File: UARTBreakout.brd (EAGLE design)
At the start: 21.6 x 16.5 mm, 0 parts

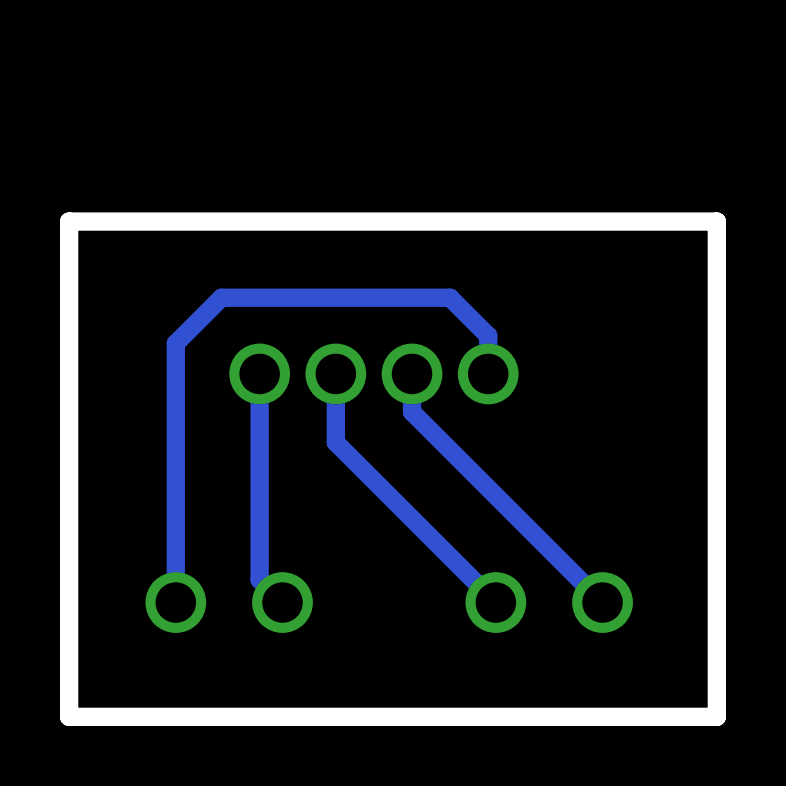
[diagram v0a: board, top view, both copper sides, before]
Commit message: Made both breakout boards REALLY aesthetic, also they self document now
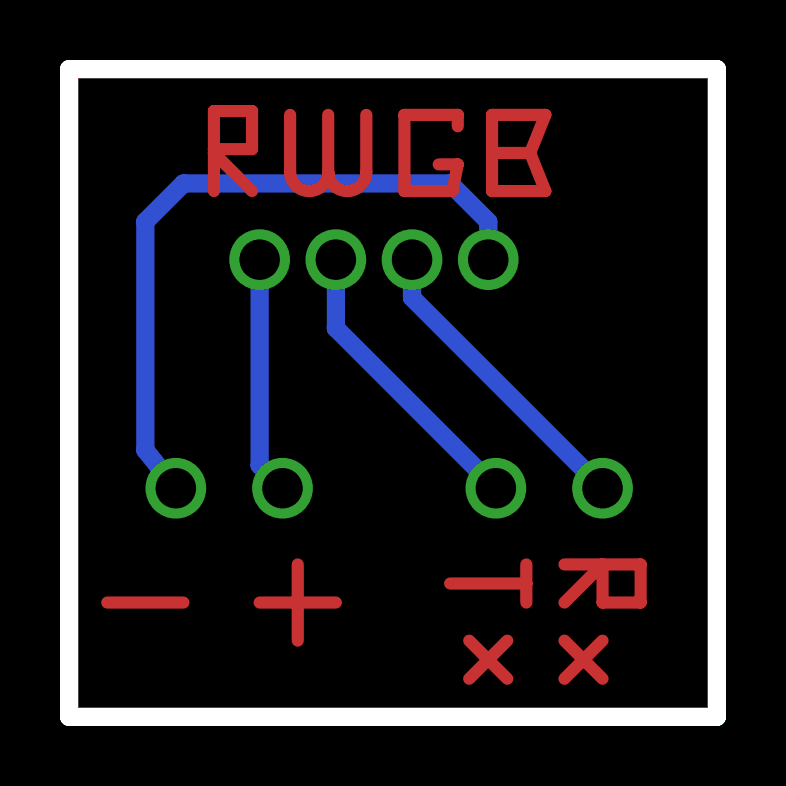
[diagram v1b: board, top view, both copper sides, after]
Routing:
- net S$9: track 0.00 -> 10.1 mm
- net S$16: track 0.00 -> 9.43 mm
- net S$7: track 0.00 -> 8.27 mm
- net S$5: track 0.00 -> 8.15 mm
- net S$8888: track 0.00 -> 7.84 mm
- net S$2: track 0.00 -> 5.08 mm
- net S$3: track 0.00 -> 3.81 mm
- net S$6: track 0.00 -> 3.59 mm
- net S$4: track 0.00 -> 3.59 mm
- net S$1: track 0.00 -> 2.54 mm
- net GND: track 21.5 -> 23.0 mm
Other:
- board size 21.6 x 16.5 mm -> 21.6 x 21.6 mm
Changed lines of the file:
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@@
 <polygon width="0.6096" layer="20">
 <vertex x="0" y="0"/>
-<vertex x="0" y="16.51"/>
-<vertex x="21.59" y="16.51"/>
+<vertex x="0" y="21.59"/>
+<vertex x="21.59" y="21.59"/>
 <vertex x="21.59" y="0"/>
 </polygon>
@@
 <signals>
 <signal name="TX">
-<via x="8.89" y="11.43" extent="1-16" drill="1.35"/>
-<via x="14.224" y="3.81" extent="1-16" drill="1.35" diameter="1.3"/>
-<wire x1="14.224" y1="3.81" x2="8.89" y2="9.144" width="0.6096" layer="16"/>
-<wire x1="8.89" y1="9.144" x2="8.89" y2="11.43" width="0.6096" layer="16"/>
+<via x="8.89" y="15.24" extent="1-16" drill="1.35"/>
+<via x="14.224" y="7.62" extent="1-16" drill="1.35" diameter="1.3"/>
+<wire x1="14.224" y1="7.62" x2="8.89" y2="12.954" width="0.6096" layer="16"/>
+<wire x1="8.89" y1="12.954" x2="8.89" y2="15.24" width="0.6096" layer="16"/>
 </signal>
 <signal name="RX">
-<via x="11.43" y="11.43" extent="1-16" drill="1.35"/>
-<via x="17.78" y="3.81" extent="1-16" drill="1.35" diameter="1.3"/>
-<wire x1="17.78" y1="3.81" x2="11.43" y2="10.16" width="0.6096" layer="16"/>
-<wire x1="11.43" y1="10.16" x2="11.43" y2="11.43" width="0.6096" layer="16"/>
+<via x="11.43" y="15.24" extent="1-16" drill="1.35"/>
+<via x="17.78" y="7.62" extent="1-16" drill="1.35" diameter="1.3"/>
+<wire x1="17.78" y1="7.62" x2="11.43" y2="13.97" width="0.6096" layer="16"/>
+<wire x1="11.43" y1="13.97" x2="11.43" y2="15.24" width="0.6096" layer="16"/>
 </signal>
 <signal name="GND">
-<via x="13.97" y="11.43" extent="1-16" drill="1.35"/>
-<via x="3.556" y="3.81" extent="1-16" drill="1.35" diameter="1.3"/>
-<wire x1="3.556" y1="3.81" x2="3.556" y2="12.446" width="0.6096" layer="16"/>
-<wire x1="3.556" y1="12.446" x2="5.08" y2="13.97" width="0.6096" layer="16"/>
-<wire x1="5.08" y1="13.97" x2="12.7" y2="13.97" width="0.6096" layer="16"/>
-<wire x1="12.7" y1="13.97" x2="13.97" y2="12.7" width="0.6096" layer="16"/>
-<wire x1="13.97" y1="12.7" x2="13.97" y2="11.43" width="0.6096" layer="16"/>
+<via x="13.97" y="15.24" extent="1-16" drill="1.35"/>
+<via x="3.556" y="7.62" extent="1-16" drill="1.35" diameter="1.3"/>
+<wire x1="3.556" y1="7.62" x2="2.54" y2="8.89" width="0.6096" layer="16"/>
+<wire x1="2.54" y1="8.89" x2="2.54" y2="16.51" width="0.6096" layer="16"/>
+<wire x1="3.81" y1="17.78" x2="2.54" y2="16.51" width="0.6096" layer="16"/>
+<wire x1="13.97" y1="15.24" x2="13.97" y2="16.51" width="0.6096" layer="16"/>
+<wire x1="13.97" y1="16.51" x2="12.7" y2="17.78" width="0.6096" layer="16"/>
+<wire x1="12.7" y1="17.78" x2="3.81" y2="17.78" width="0.6096" layer="16"/>
 </signal>
 <signal name="VCC">
-<via x="6.35" y="11.43" extent="1-16" drill="1.35"/>
-<via x="7.112" y="3.81" extent="1-16" drill="1.35" diameter="1.3"/>
-<wire x1="7.112" y1="3.81" x2="6.35" y2="4.572" width="0.6096" layer="16"/>
-<wire x1="6.35" y1="4.572" x2="6.35" y2="11.43" width="0.6096" layer="16"/>
+<via x="6.35" y="15.24" extent="1-16" drill="1.35"/>
+<via x="7.112" y="7.62" extent="1-16" drill="1.35" diameter="1.3"/>
+<wire x1="7.112" y1="7.62" x2="6.35" y2="8.382" width="0.6096" layer="16"/>
+<wire x1="6.35" y1="8.382" x2="6.35" y2="15.24" width="0.6096" layer="16"/>
+</signal>
+<signal name="S$1">
+<wire x1="1.27" y1="3.81" x2="3.81" y2="3.81" width="0.4064" layer="1"/>
+</signal>
+<signal name="S$2">
+<wire x1="6.35" y1="3.81" x2="7.62" y2="3.81" width="0.4064" layer="1"/>
+<wire x1="7.62" y1="5.08" x2="7.62" y2="3.81" width="0.4064" layer="1"/>
+<wire x1="8.89" y1="3.81" x2="7.62" y2="3.81" width="0.4064" layer="1"/>
+<wire x1="7.62" y1="2.54" x2="7.62" y2="3.81" width="0.4064" layer="1"/>
+</signal>
+<signal name="S$5">
+<wire x1="16.51" y1="5.08" x2="17.78" y2="5.08" width="0.4064" layer="1"/>
+<wire x1="19.05" y1="5.08" x2="19.05" y2="3.81" width="0.4064" layer="1"/>
+<wire x1="19.05" y1="3.81" x2="17.78" y2="3.81" width="0.4064" layer="1"/>
+<wire x1="17.78" y1="5.08" x2="16.51" y2="3.81" width="0.4064" layer="1"/>
+<wire x1="17.78" y1="3.81" x2="17.78" y2="5.08" width="0.4064" layer="1"/>
+<wire x1="17.78" y1="5.08" x2="19.05" y2="5.08" width="0.4064" layer="1"/>
+</signal>
+<signal name="S$6">
+<wire x1="16.51" y1="2.54" x2="17.78" y2="1.27" width="0.4064" layer="1"/>
+<wire x1="16.51" y1="1.27" x2="17.78" y2="2.54" width="0.4064" layer="1"/>
+<wire x1="16.51" y1="1.27" x2="16.51" y2="2.54" width="0" layer="19" extent="1-1"/>
+</signal>
+<signal name="S$3">
+<wire x1="12.7" y1="4.445" x2="15.24" y2="4.445" width="0.4064" layer="1"/>
+<wire x1="15.24" y1="4.445" x2="15.24" y2="5.08" width="0.4064" layer="1"/>
+<wire x1="15.24" y1="4.445" x2="15.24" y2="3.81" width="0.4064" layer="1"/>
+</signal>
+<signal name="S$4">
+<wire x1="13.335" y1="2.54" x2="13.97" y2="1.905" width="0.4064" layer="1"/>
+<wire x1="14.605" y1="1.27" x2="13.97" y2="1.905" width="0.4064" layer="1"/>
+<wire x1="14.605" y1="2.54" x2="13.97" y2="1.905" width="0.4064" layer="1"/>
+<wire x1="13.97" y1="1.905" x2="13.335" y2="1.27" width="0.4064" layer="1"/>
+</signal>
+<signal name="S$7">
+<wire x1="4.826" y1="17.526" x2="4.826" y2="18.796" width="0.4064" layer="1"/>
+<wire x1="4.826" y1="20.193" x2="6.096" y2="20.193" width="0.4064" layer="1"/>
+<wire x1="6.096" y1="20.193" x2="6.096" y2="18.923" width="0.4064" layer="1"/>
+<wire x1="4.826" y1="18.796" x2="6.096" y2="17.526" width="0.4064" layer="1"/>
+<wire x1="4.826" y1="18.796" x2="4.826" y2="18.923" width="0.4064" layer="1"/>
+<wire x1="4.826" y1="20.193" x2="4.826" y2="18.923" width="0.4064" layer="1"/>
+<wire x1="4.826" y1="18.923" x2="6.096" y2="18.923" width="0.4064" layer="1"/>
+</signal>
+<signal name="S$16">
+<wire x1="7.366" y1="18.161" x2="8.001" y2="17.526" width="0.4064" layer="1" curve="90"/>
+<wire x1="8.001" y1="17.526" x2="8.636" y2="18.161" width="0.4064" layer="1" curve="90"/>
+<wire x1="8.636" y1="18.161" x2="9.271" y2="17.526" width="0.4064" layer="1" curve="90"/>
+<wire x1="9.271" y1="17.526" x2="9.906" y2="18.161" width="0.4064" layer="1" curve="90"/>
+<wire x1="7.366" y1="18.161" x2="7.366" y2="20.066" width="0.4064" layer="1"/>
+<wire x1="9.906" y1="18.161" x2="9.906" y2="20.066" width="0.4064" layer="1"/>
+<wire x1="8.636" y1="18.034" x2="8.636" y2="20.066" width="0.4064" layer="1"/>
+<wire x1="8.636" y1="18.161" x2="8.636" y2="18.034" width="0" layer="19" extent="1-1"/>
+</signal>
+<signal name="S$8888">
+<wire x1="12.954" y1="20.066" x2="11.176" y2="20.066" width="0.4064" layer="1"/>
+<wire x1="11.176" y1="20.066" x2="11.176" y2="17.526" width="0.4064" layer="1"/>
+<wire x1="11.176" y1="17.526" x2="12.7762" y2="17.526" width="0.4064" layer="1"/>
+<wire x1="12.7762" y1="17.526" x2="12.954" y2="18.415" width="0.4064" layer="1"/>
+<wire x1="12.954" y1="20.066" x2="12.954" y2="19.685" width="0.4064" layer="1"/>
+<wire x1="12.319" y1="18.415" x2="12.954" y2="18.415" width="0.4064" layer="1"/>
+</signal>
+<signal name="S$9">
+<wire x1="14.097" y1="18.796" x2="14.097" y2="17.526" width="0.4064" layer="1"/>
+<wire x1="14.097" y1="17.526" x2="15.875" y2="17.526" width="0.4064" layer="1"/>
+<wire x1="15.875" y1="17.526" x2="15.367" y2="18.796" width="0.4064" layer="1"/>
+<wire x1="15.367" y1="18.796" x2="15.875" y2="20.066" width="0.4064" layer="1"/>
+<wire x1="15.875" y1="20.066" x2="14.097" y2="20.066" width="0.4064" layer="1"/>
+<wire x1="14.097" y1="20.066" x2="14.097" y2="18.796" width="0.4064" layer="1"/>
+<wire x1="14.097" y1="18.796" x2="15.367" y2="18.796" width="0.4064" layer="1"/>
 </signal>
 </signals>
